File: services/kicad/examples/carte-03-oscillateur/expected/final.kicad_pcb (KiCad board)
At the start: 2 copper layers, 50 x 35 mm, 15 parts, among them J1 PWR, J2 OUT, U1 NE555

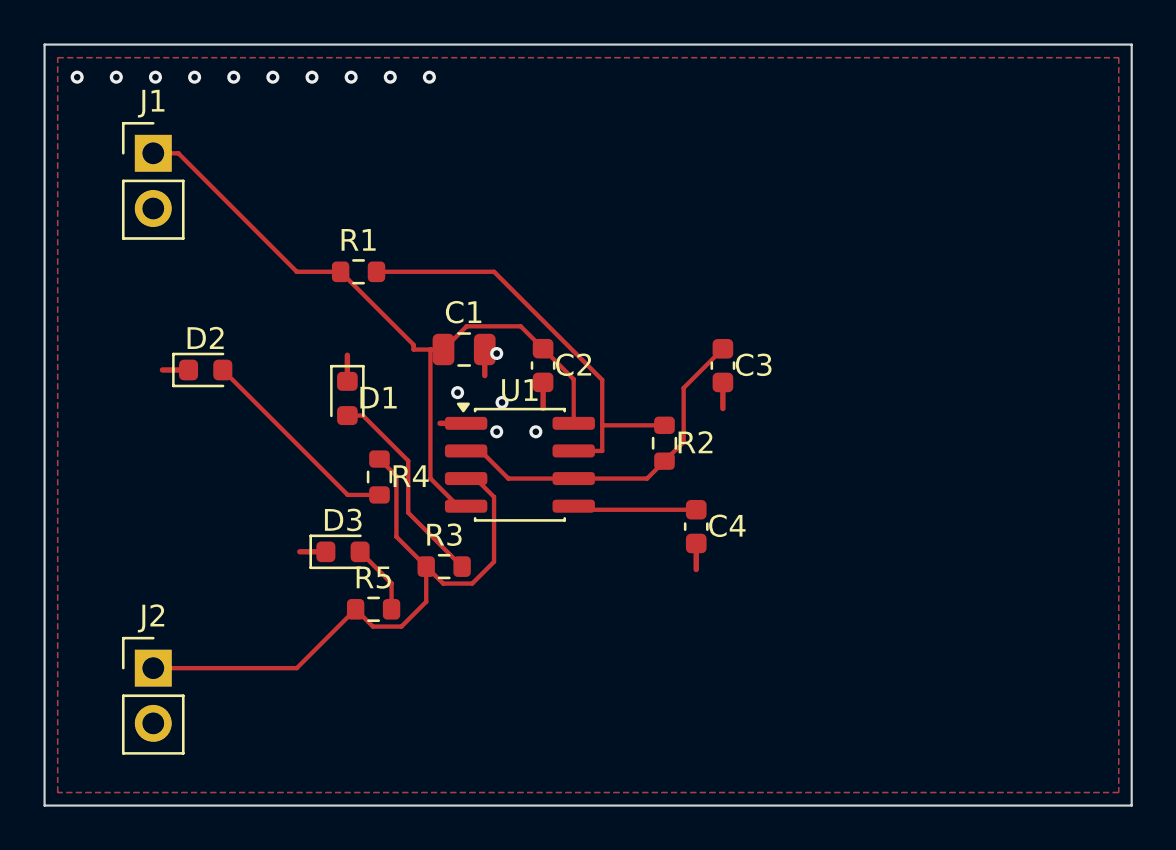
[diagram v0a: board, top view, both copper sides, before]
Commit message: fix(routing): GND route par defaut, plan sur reglage -- sites et tests alignes
Quatre sites de routing.py lisaient encore `_nets_confies_au_plan()` au
lieu de la constante `_NETS_CONFIES_AU_PLAN` que le module reaffecte et que
les tests remplacent : le reglage n atteignait pas ces sites. L escalade
n avait plus de repli vers `_NETS_DE_PLAN_CONNUS` (une connexion GND
manquante doit pouvoir escalader quand GND est route).

Tests encodant l ancienne strategie (GND confie au plan) recrits : les deux
cas sont couverts, GND route par defaut (decision utilisateur du 2026-09-10,
reference STM32 Astra + docs/methodologie-routage.md) et GND confie au plan
sur le reglage `gnd_confie_au_plan`.

`_reattribuer_les_decouplages` rend intact ce qui n est pas une liste.
Deux tests de journal Freerouting comparaient un chemin Windows a un
entrypoint POSIX : `as_posix()`.

Cartes 01, 02, 03, 04, 06 regenerees avec GND route : 100 % routees,
0 erreur DRC, fabricables ; placement.kicad_pcb livre pour chacune.

1630 passed, 2 skipped.

Co-Authored-By: Claude Fable 5.1 <noreply@anthropic.com>
Claude-Session: https://claude.ai/code/session_01TnMqm4La2CxQHHB5K8aSSV
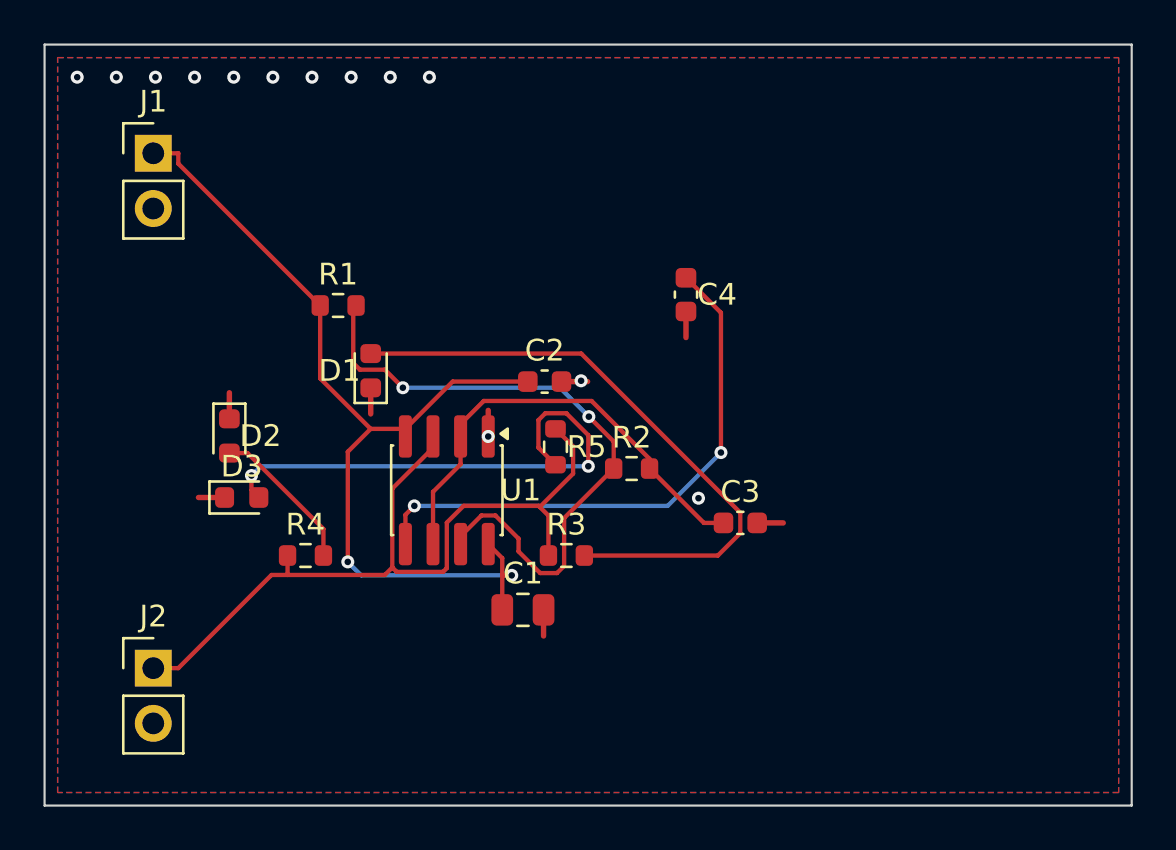
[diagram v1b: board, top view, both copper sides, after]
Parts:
- moved C1 12.3 mm to (145.5, 113.5)
- moved R5 11.2 mm to (147.0, 106.0), turned to -90 degrees
- moved C4 10.7 mm to (153.0, 99.0)
- moved C3 7.28 mm to (155.5, 109.5), turned to 0 degrees
- moved R3 5.64 mm to (147.5, 111.0)
- moved D3 5.29 mm to (132.6, 108.3)
- moved R4 4.96 mm to (135.5, 111.0), turned to 0 degrees
- moved U1 3.56 mm to (142.0, 108.0), turned to -90 degrees
- moved D2 3.22 mm to (132.0, 105.5), turned to -90 degrees
- moved R2 1.91 mm to (150.5, 107.0), turned to 0 degrees
- moved R1 1.81 mm to (137.0, 99.5)
- moved D1 1.67 mm to (138.5, 102.5), turned to 90 degrees
- moved C2 0.74 mm to (146.5, 103.0), turned to 0 degrees
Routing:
- net LED3_A: track 3.24 -> 23.5 mm, vias 0 -> 2
- net CTRL: track 5.70 -> 25.8 mm, vias 0 -> 2
- net LED1_A: track 9.55 -> 28.6 mm
- net DISCH: track 19.9 -> 29.9 mm, vias 0 -> 2
- net VCC: track 34.8 -> 44.0 mm, vias 0 -> 2
- net OUT: track 30.4 -> 36.9 mm
- net THRES: track 16.3 -> 21.2 mm
- net LED2_A: track 9.59 -> 6.99 mm
- net GND: vias 15 -> 13
